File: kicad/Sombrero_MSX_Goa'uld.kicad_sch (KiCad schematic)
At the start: 16 parts, among them J1 Z80CPU, U1 74AHCT373, U2 74AHCT373, U3 SN74LVC245AN, U4 SN74LVC245AN, U5 SN74LVC245AN, U6 Tang_Nano_20k

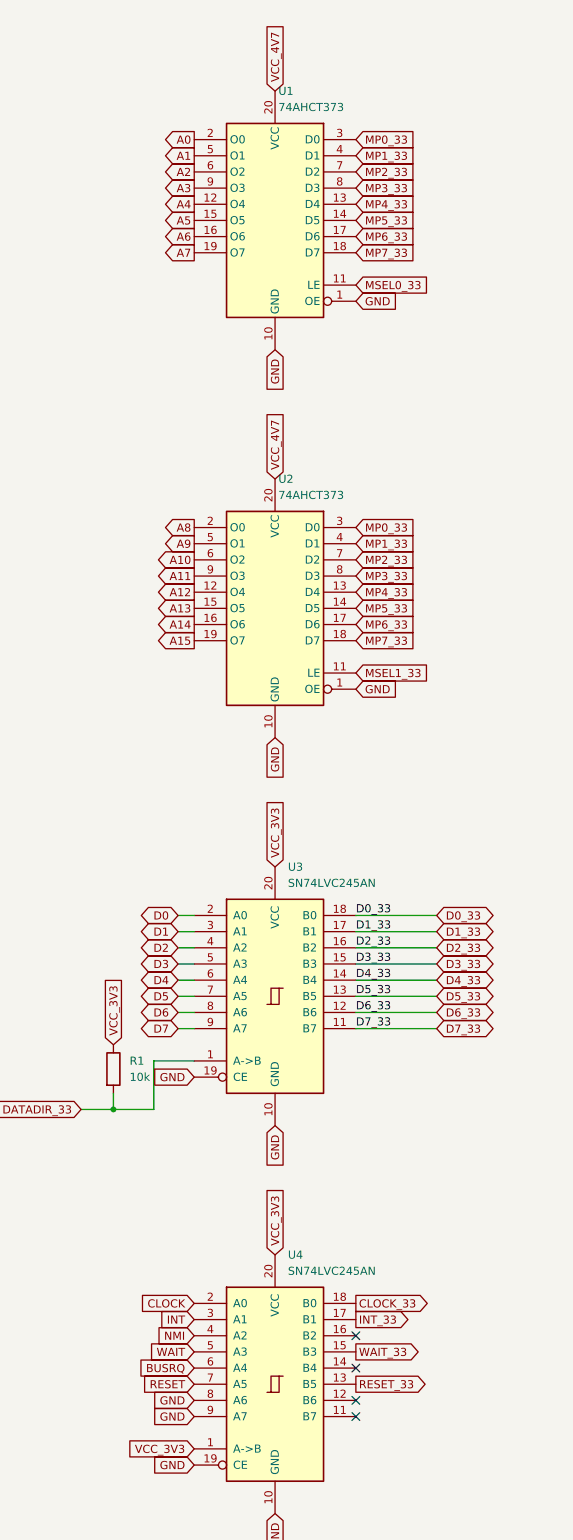
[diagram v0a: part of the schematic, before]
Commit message: Removed NMI, BUSRQ pins to avoid overheating of U4 due to voltage >> 5V Fixed name 74HCT373
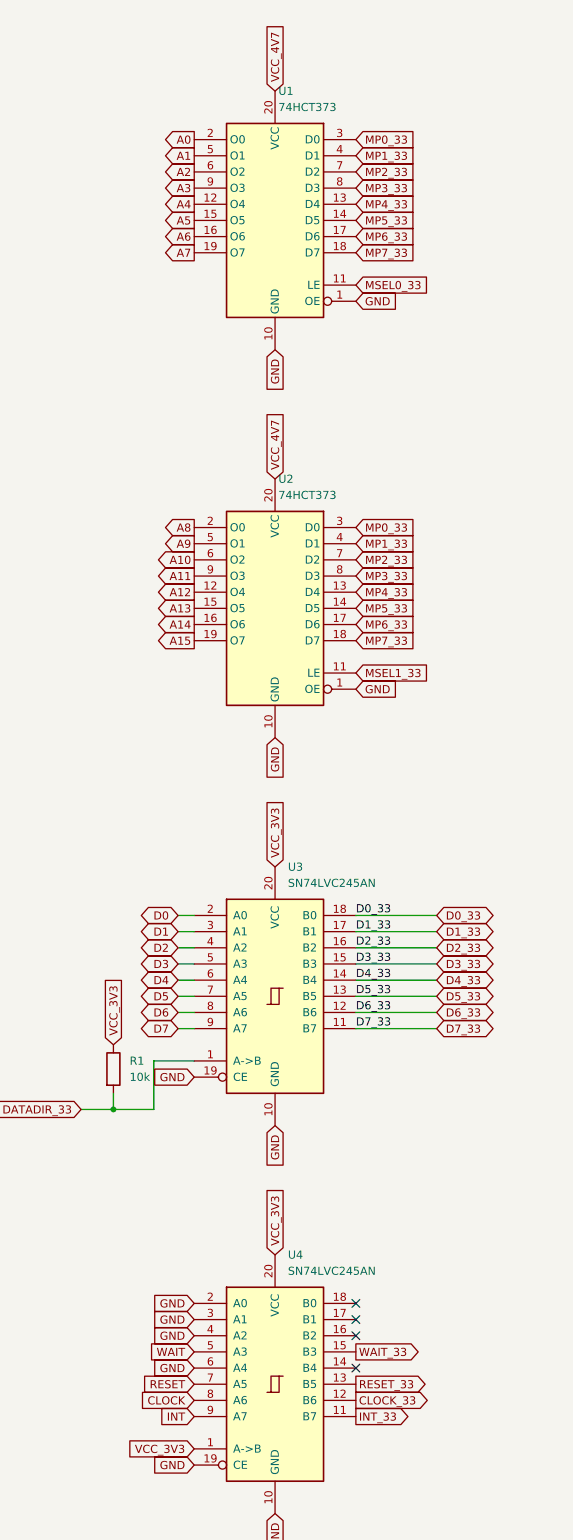
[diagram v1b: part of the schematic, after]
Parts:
- U1, U2: value 74AHCT373 -> 74HCT373
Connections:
- net BUSRQ: no longer U4.6 (A4)
- net CLOCK: now also U4.8 (A6); no longer U4.2 (A0)
- net CLOCK_33: now also U4.12 (B6); no longer U4.18 (B0)
- net GND: now also U4.2 (A0), U4.3 (A1), U4.4 (A2), U4.6 (A4); no longer U4.8 (A6), U4.9 (A7)
- net INT: now also U4.9 (A7); no longer U4.3 (A1)
- net INT_33: now also U4.11 (B7); no longer U4.17 (B1)
- net NMI: no longer U4.4 (A2)
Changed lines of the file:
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@@
   (no_connect (at 297.18 120.65))
   (no_connect (at 368.3 123.19))
-  (no_connect (at 229.87 237.49))
   (no_connect (at 320.04 69.85))
+  (no_connect (at 229.87 222.25))
   (no_connect (at 297.18 125.73))
   (no_connect (at 229.87 229.87))
   (no_connect (at 297.18 123.19))
+  (no_connect (at 229.87 219.71))
   (no_connect (at 229.87 224.79))
-  (no_connect (at 229.87 234.95))
   (no_connect (at 320.04 67.31))
   (wire (pts (xy 201.93 173.99) (xy 204.47 173.99))
@@
     )
   )
-  (global_label "BUSRQ" (shape input) (at 204.47 229.87 180) (fields_autoplaced)
-    (effects (font (size 1.27 1.27)) (justify right))
-    (property "Intersheet References" "${INTERSHEET_REFS}" (id 0) (at 195.7353 229.7906 0)
-      (effects (font (size 1.27 1.27)) (justify right) hide)
-    )
-  )
   (global_label "WR" (shape input) (at 92.71 129.54 180) (fields_autoplaced)
     (effects (font (size 1.27 1.27)) (justify right))
@@
     )
   )
+  (global_label "GND" (shape input) (at 204.47 229.87 180) (fields_autoplaced)
+    (effects (font (size 1.27 1.27)) (justify right))
+    (property "Intersheet References" "${INTERSHEET_REFS}" (id 0) (at 198.2753 229.7906 0)
+      (effects (font (size 1.27 1.27)) (justify right) hide)
+    )
+  )
   (global_label "A4" (shape input) (at 128.27 93.98 0) (fields_autoplaced)
     (effects (font (size 1.27 1.27)) (justify left))
@@
     )
   )
-  (global_label "CLOCK_33" (shape output) (at 229.87 219.71 0) (fields_autoplaced)
-    (effects (font (size 1.27 1.27)) (justify left))
-    (property "Intersheet References" "${INTERSHEET_REFS}" (id 0) (at 241.7494 219.6306 0)
+  (global_label "CLOCK_33" (shape output) (at 229.87 234.95 0) (fields_autoplaced)
+    (effects (font (size 1.27 1.27)) (justify left))
+    (property "Intersheet References" "${INTERSHEET_REFS}" (id 0) (at 241.7494 234.8706 0)
       (effects (font (size 1.27 1.27)) (justify left) hide)
     )
@@
     )
   )
-  (global_label "CLOCK" (shape input) (at 204.47 219.71 180) (fields_autoplaced)
-    (effects (font (size 1.27 1.27)) (justify right))
-    (property "Intersheet References" "${INTERSHEET_REFS}" (id 0) (at 195.9772 219.6306 0)
+  (global_label "CLOCK" (shape input) (at 204.47 234.95 180) (fields_autoplaced)
+    (effects (font (size 1.27 1.27)) (justify right))
+    (property "Intersheet References" "${INTERSHEET_REFS}" (id 0) (at 195.9772 234.8706 0)
       (effects (font (size 1.27 1.27)) (justify right) hide)
     )
@@
     )
   )
-  (global_label "INT" (shape input) (at 204.47 222.25 180) (fields_autoplaced)
-    (effects (font (size 1.27 1.27)) (justify right))
-    (property "Intersheet References" "${INTERSHEET_REFS}" (id 0) (at 199.2429 222.1706 0)
+  (global_label "INT" (shape input) (at 204.47 237.49 180) (fields_autoplaced)
+    (effects (font (size 1.27 1.27)) (justify right))
+    (property "Intersheet References" "${INTERSHEET_REFS}" (id 0) (at 199.2429 237.4106 0)
       (effects (font (size 1.27 1.27)) (justify right) hide)
     )
@@
     )
   )
+  (global_label "GND" (shape input) (at 204.47 224.79 180) (fields_autoplaced)
+    (effects (font (size 1.27 1.27)) (justify right))
+    (property "Intersheet References" "${INTERSHEET_REFS}" (id 0) (at 198.2753 224.7106 0)
+      (effects (font (size 1.27 1.27)) (justify right) hide)
+    )
+  )
   (global_label "GND" (shape input) (at 368.3 151.13 0) (fields_autoplaced)
     (effects (font (size 1.27 1.27)) (justify left))
@@
     )
   )
-  (global_label "GND" (shape input) (at 204.47 234.95 180) (fields_autoplaced)
-    (effects (font (size 1.27 1.27)) (justify right))
-    (property "Intersheet References" "${INTERSHEET_REFS}" (id 0) (at 198.2753 234.8706 0)
-      (effects (font (size 1.27 1.27)) (justify right) hide)
-    )
-  )
   (global_label "A4" (shape output) (at 204.47 46.99 180) (fields_autoplaced)
     (effects (font (size 1.27 1.27)) (justify right))
@@
     )
   )
+  (global_label "GND" (shape input) (at 204.47 219.71 180) (fields_autoplaced)
+    (effects (font (size 1.27 1.27)) (justify right))
+    (property "Intersheet References" "${INTERSHEET_REFS}" (id 0) (at 198.2753 219.6306 0)
+      (effects (font (size 1.27 1.27)) (justify right) hide)
+    )
+  )
   (global_label "A3" (shape output) (at 204.47 44.45 180) (fields_autoplaced)
     (effects (font (size 1.27 1.27)) (justify right))
@@
     )
   )
-  (global_label "INT_33" (shape output) (at 229.87 222.25 0) (fields_autoplaced)
-    (effects (font (size 1.27 1.27)) (justify left))
-    (property "Intersheet References" "${INTERSHEET_REFS}" (id 0) (at 238.4837 222.1706 0)
+  (global_label "INT_33" (shape output) (at 229.87 237.49 0) (fields_autoplaced)
+    (effects (font (size 1.27 1.27)) (justify left))
+    (property "Intersheet References" "${INTERSHEET_REFS}" (id 0) (at 238.4837 237.4106 0)
       (effects (font (size 1.27 1.27)) (justify left) hide)
     )
@@
     )
   )
-  (global_label "GND" (shape input) (at 204.47 237.49 180) (fields_autoplaced)
-    (effects (font (size 1.27 1.27)) (justify right))
-    (property "Intersheet References" "${INTERSHEET_REFS}" (id 0) (at 198.2753 237.4106 0)
-      (effects (font (size 1.27 1.27)) (justify right) hide)
-    )
-  )
   (global_label "WAIT_33" (shape input) (at 297.18 133.35 180) (fields_autoplaced)
     (effects (font (size 1.27 1.27)) (justify right))
@@
     )
   )
-  (global_label "NMI" (shape input) (at 204.47 224.79 180) (fields_autoplaced)
-    (effects (font (size 1.27 1.27)) (justify right))
-    (property "Intersheet References" "${INTERSHEET_REFS}" (id 0) (at 198.7591 224.7106 0)
-      (effects (font (size 1.27 1.27)) (justify right) hide)
-    )
-  )
   (global_label "MP0_33" (shape input) (at 229.87 36.83 0) (fields_autoplaced)
     (effects (font (size 1.27 1.27)) (justify left))
@@
     (property "Intersheet References" "${INTERSHEET_REFS}" (id 0) (at 133.0737 139.6206 0)
       (effects (font (size 1.27 1.27)) (justify left) hide)
+    )
+  )
+  (global_label "GND" (shape input) (at 204.47 222.25 180) (fields_autoplaced)
+    (effects (font (size 1.27 1.27)) (justify right))
+    (property "Intersheet References" "${INTERSHEET_REFS}" (id 0) (at 198.2753 222.1706 0)
+      (effects (font (size 1.27 1.27)) (justify right) hide)
     )
   )
@@
       (effects (font (size 1.27 1.27)) (justify right))
     )
-    (property "Value" "74AHCT373" (id 1) (at 217.6906 31.75 0)
+    (property "Value" "74HCT373" (id 1) (at 217.6906 31.75 0)
       (effects (font (size 1.27 1.27)) (justify right))
     )
@@
       (effects (font (size 1.27 1.27)) (justify right))
     )
-    (property "Value" "74AHCT373" (id 1) (at 217.6906 92.71 0)
+    (property "Value" "74HCT373" (id 1) (at 217.6906 92.71 0)
       (effects (font (size 1.27 1.27)) (justify right))
     )
@@
     )
     (path "/5897a603-0fa6-4397-ac51-eb0b10de3ce5"
-      (reference "U1") (unit 1) (value "74AHCT373") (footprint "Package_DIP:DIP-20_W7.62mm_LongPads")
+      (reference "U1") (unit 1) (value "74HCT373") (footprint "Package_DIP:DIP-20_W7.62mm_LongPads")
     )
     (path "/e92cc35f-37c7-4c09-ba6c-54074ae951a7"
-      (reference "U2") (unit 1) (value "74AHCT373") (footprint "Package_DIP:DIP-20_W7.62mm_LongPads")
+      (reference "U2") (unit 1) (value "74HCT373") (footprint "Package_DIP:DIP-20_W7.62mm_LongPads")
     )
     (path "/84b63230-a70d-4332-a0e1-11d8769313a9"
